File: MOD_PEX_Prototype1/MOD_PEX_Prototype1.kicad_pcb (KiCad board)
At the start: 2 copper layers, 78.4 x 40 mm, 66 parts, among them CN1 CONN_PANNEL_2X2, CN2 CONN_PANNEL_2X2, J1 RJ45_CHAIN, J2 RJ45_CHAIN, P1 HEADER_3X1, P2 HEADER_5X1, P3 HEADER_5X2, P4 HEADER_2X1, Q1 MMBT3904, Q2 MMBT3904, SW1 SWITCH_HH, U1 LPC111X_LQFP48, U2 AP1117E50G, U3 AP1117E33G, U4 SN75176BDR, X1 10MHz

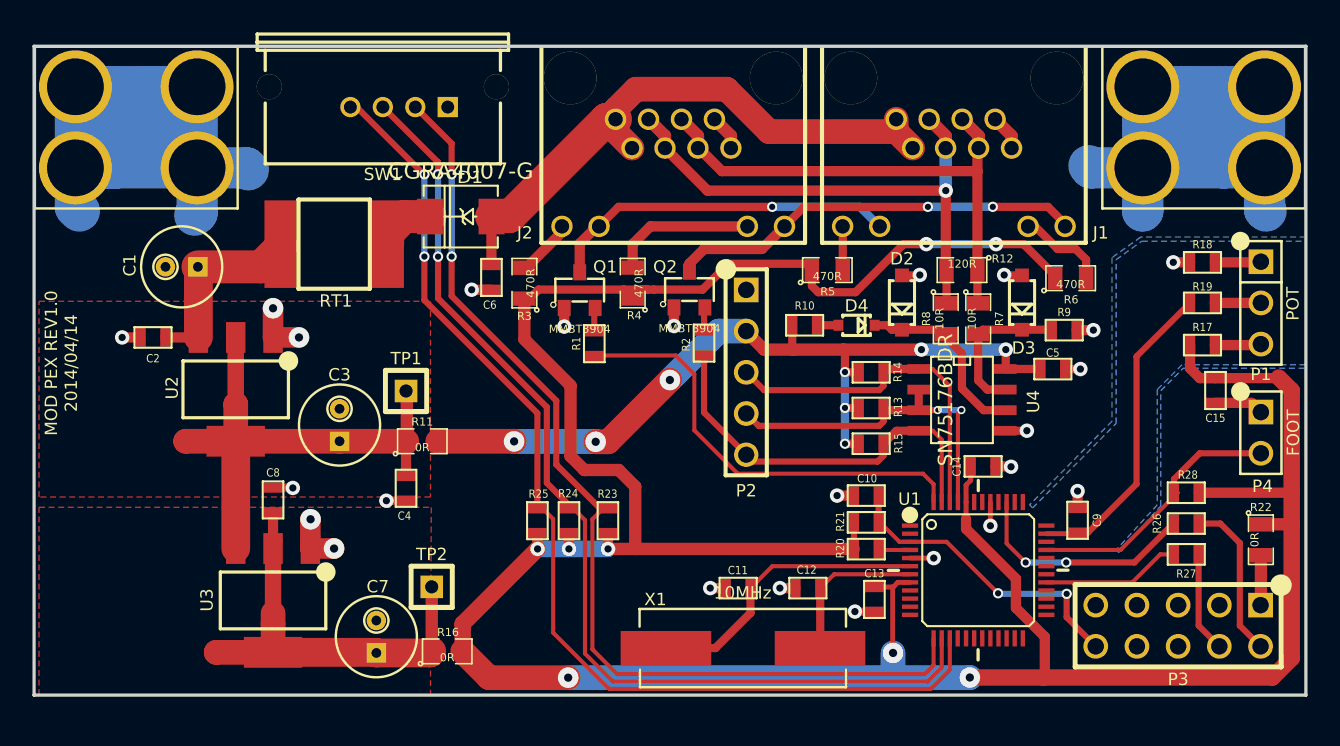
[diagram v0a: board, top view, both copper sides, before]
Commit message: updating footprints (to use the ones from the mod-kicad-footprints repository)
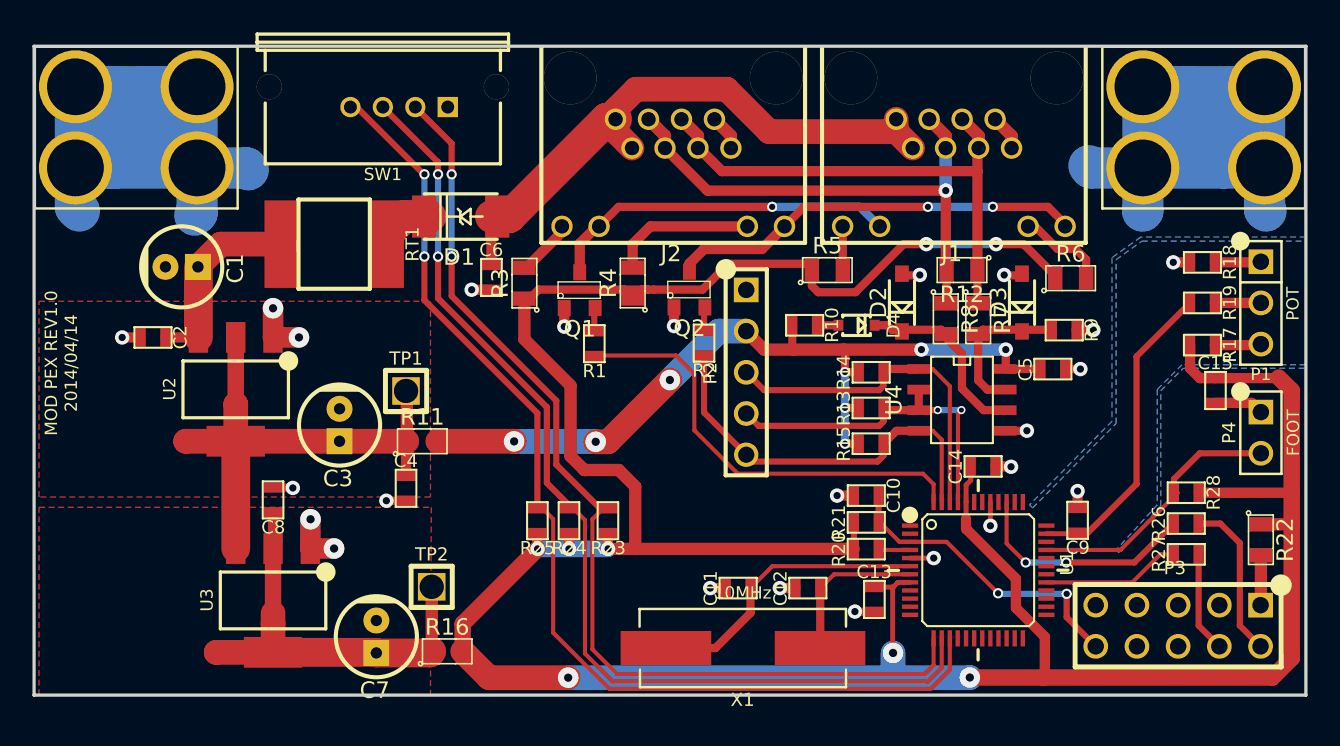
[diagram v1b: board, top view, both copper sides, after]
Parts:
- C1, C3, C7: footprint CAP_RAD_5MM -> MOD_Footprints_Lib:CAP_RAD_5MM
- C10, C11, C12, C13, C14, C15, C2, C4, C5, C6, C8, C9, R1, R10, R13, R14, R15, R17, R18, R19, R2, R20, R21, R23, R24, R25, R26, R27, R28, R9: footprint SM0603 -> MOD_Footprints_Lib:SM0603
- CN1, CN2: footprint CONN_PANNEL -> MOD_Footprints_Lib:CONN_PANNEL
- D1: footprint DO-214AC(SMA) -> MOD_Footprints_Lib:DO-214AC(SMA)
- D2, D3: footprint SOD123 -> MOD_Footprints_Lib:SOD123
- D4: footprint SOD323 -> MOD_Footprints_Lib:SOD323
- J1, J2: footprint RJ45-RJHSE5084 -> MOD_Footprints_Lib:RJ45-RJHSE5084
- P1: footprint PIN_ARRAY_3X1 -> MOD_Footprints_Lib:PIN_ARRAY_3X1
- P2: footprint PIN_ARRAY_5x1 -> MOD_Footprints_Lib:PIN_ARRAY_5x1
- P3: footprint PIN_ARRAY_5x2 -> MOD_Footprints_Lib:PIN_ARRAY_5x2
- P4: footprint PIN_ARRAY_2X1 -> MOD_Footprints_Lib:PIN_ARRAY_2X1
- Q1, Q2: footprint SOT23 -> MOD_Footprints_Lib:SOT23
- R11, R12, R16, R22, R3, R4, R5, R6, R7, R8: footprint SM0805 -> MOD_Footprints_Lib:SM0805
- RT1: footprint SM2920 -> MOD_Footprints_Lib:SM2920
- SW1: footprint SWITCH_HH_SK-13D26-G-6.5-K-GY -> MOD_Footprints_Lib:SWITCH_HH_SK-13D26-G-6_5-K-GY
- TP1, TP2: footprint SIL-1 -> MOD_Footprints_Lib:SIL-1
- U1: footprint LQFP48 -> MOD_Footprints_Lib:LQFP48
- U2, U3: footprint SOT223_3 -> MOD_Footprints_Lib:SOT223_3
- U4: footprint SO8E -> MOD_Footprints_Lib:SO8E
- X1: footprint HC_49US -> MOD_Footprints_Lib:HC_49US
